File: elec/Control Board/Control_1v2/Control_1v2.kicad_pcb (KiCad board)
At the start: 2 copper layers, 205 x 190 mm, 348 parts, among them J1 DB9_Female_MountingHoles, J10 Conn_02x12_Odd_Even, J11 Con_01x02_2.5mm, J12 Con_01x02_2.5mm, J13 Con_01x02_2.5mm, J14 Conn_01x10, J15 DB25_Female_MountingHoles, J16 Conn_01x04, J17 Conn_01x05, J18 Conn_01x04, J19 Conn_01x07, J2 Conn_01x08, J20 Conn_01x04_KK-254_0470531000, J201 Con_01x02_2.5mm, J23 0.100_2Pin, J24 Conn_01x04, J25 Con_01x02_2.5mm, J26 Conn_01x10, J27 Conn_02x12_Odd_Even, J28 Con_01x02_2.5mm, J29 Conn_01x10, J3 Conn_01x08, J30 Con_01x02_2.5mm, J31 Con_01x02_2.5mm, J32 Con_01x02_2.5mm, J33 Con_01x02_2.5mm, J34 Con_01x02_2.5mm, J35 Conn_02x05_Odd_Even, J36 Conn_02x05_Odd_Even, J37 Conn_01x04, J38 Conn_02x06_Odd_Even, J39 Conn_02x06_Odd_Even, J4 Conn_01x08, J40 Conn_02x06_Odd_Even, J41 Conn_02x06_Odd_Even, J42 Conn_02x06_Odd_Even, J43 Conn_01x30, J44 Conn_01x30, J45 Conn_01x30, J46 Conn_01x30, J47 Conn_01x30, J48 Conn_01x30, J49 Conn_01x30, J5 Conn_01x08, J50 Conn_01x30, J51 Conn_01x30, J52 Conn_01x30, J53 Conn_01x30, J54 Conn_01x30, J55 Conn_02x06_Odd_Even, J56 Conn_02x06_Odd_Even, J57 Conn_02x06_Odd_Even, J58 Conn_02x06_Odd_Even, J59 Conn_02x06_Odd_Even, J6 Conn_01x08, J7 Conn_01x10, J8 Conn_02x18_Odd_Even, J801 Conn_01x03_0.1", J802 Con_01x02_0.1", J803 Screw_Terminal_01x04_5.08mm, J804 Screw_Terminal_01x02_5.08mm, J805 Con_01x02_0.1", J9 Conn_01x10, K801 Relay SRU-12VDC, Q1 BSS138, Q10 BSS138, Q11 BSS138, Q12 BSS138, Q13 BSS138, Q14 BSS138, Q2 NCE01P30K, Q3 BSS138, Q4 BSS138, Q801 BSS138, Q9 BSS138

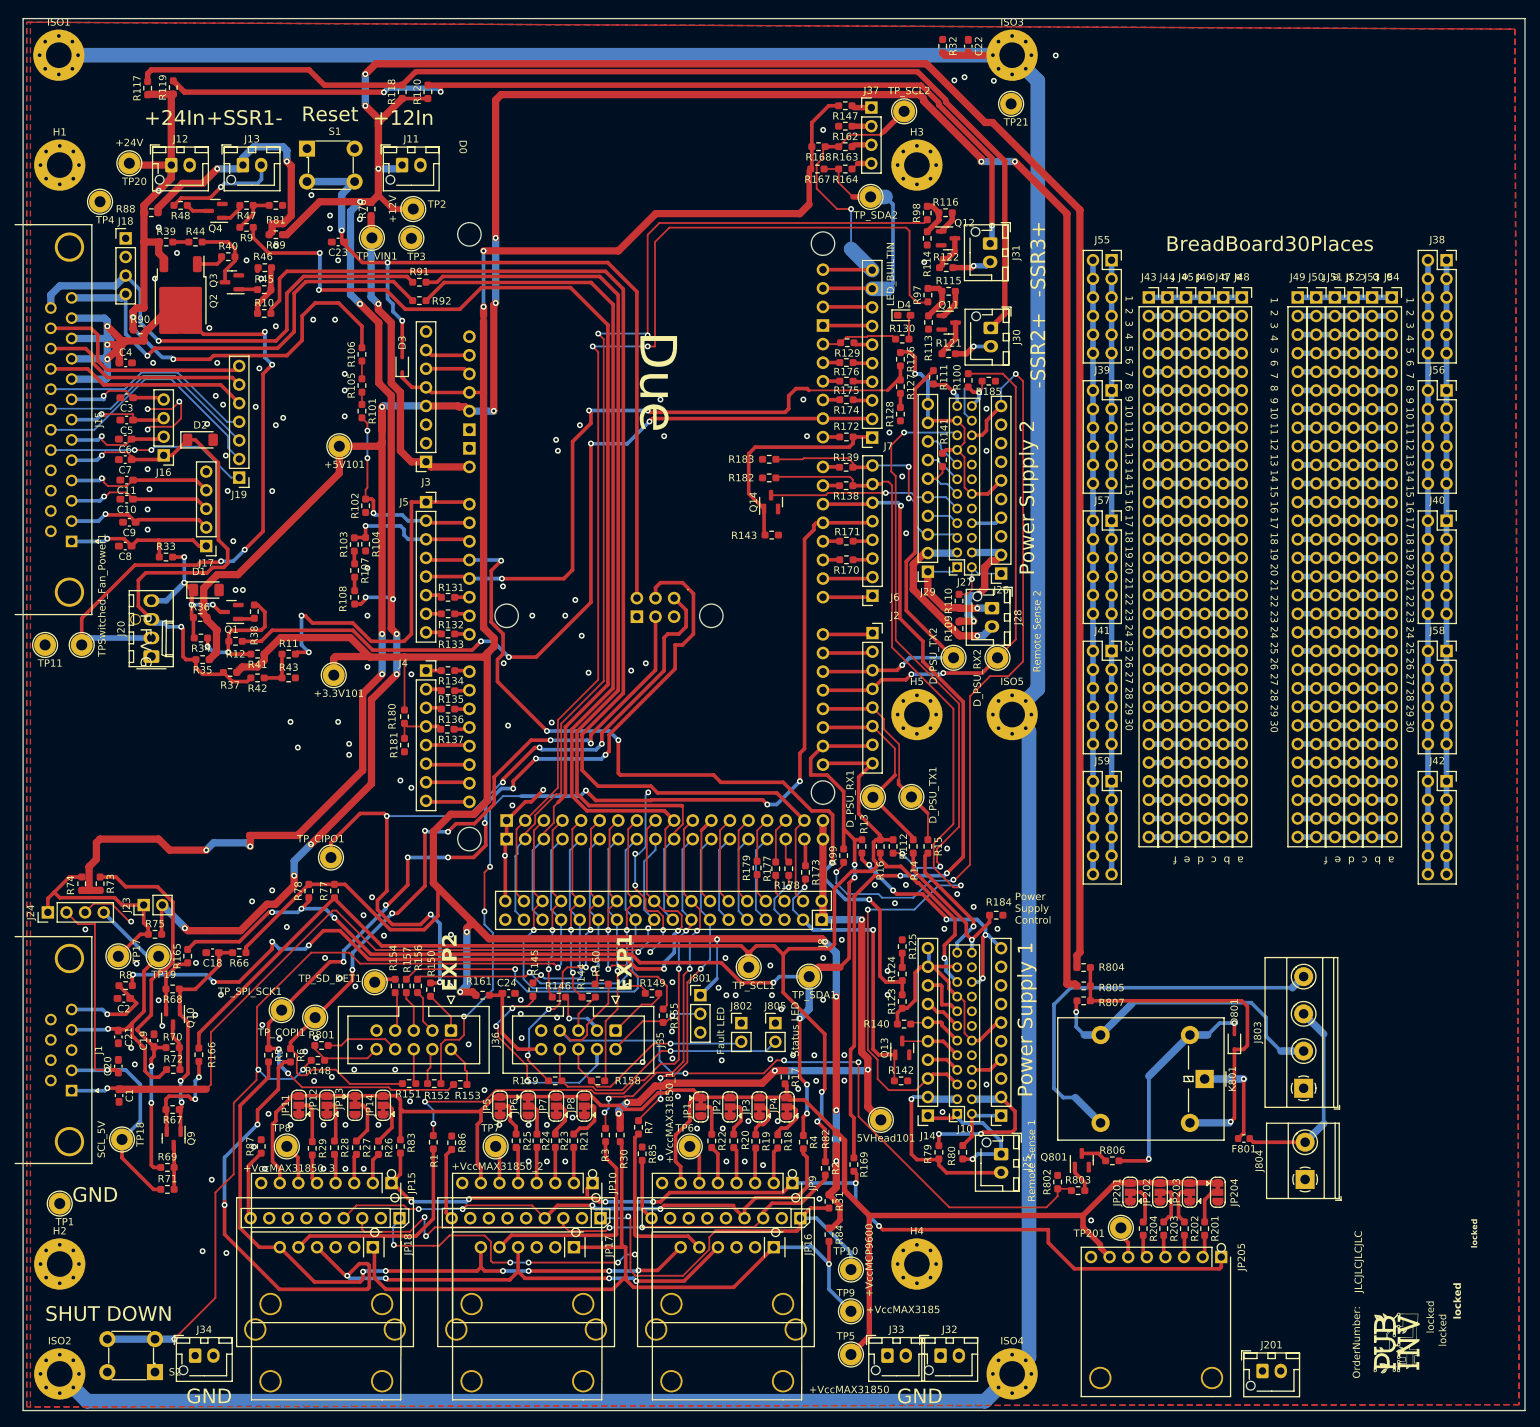
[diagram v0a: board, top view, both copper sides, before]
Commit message: PCB V1.2. Clear PCB errors. Plenty of warnings still.
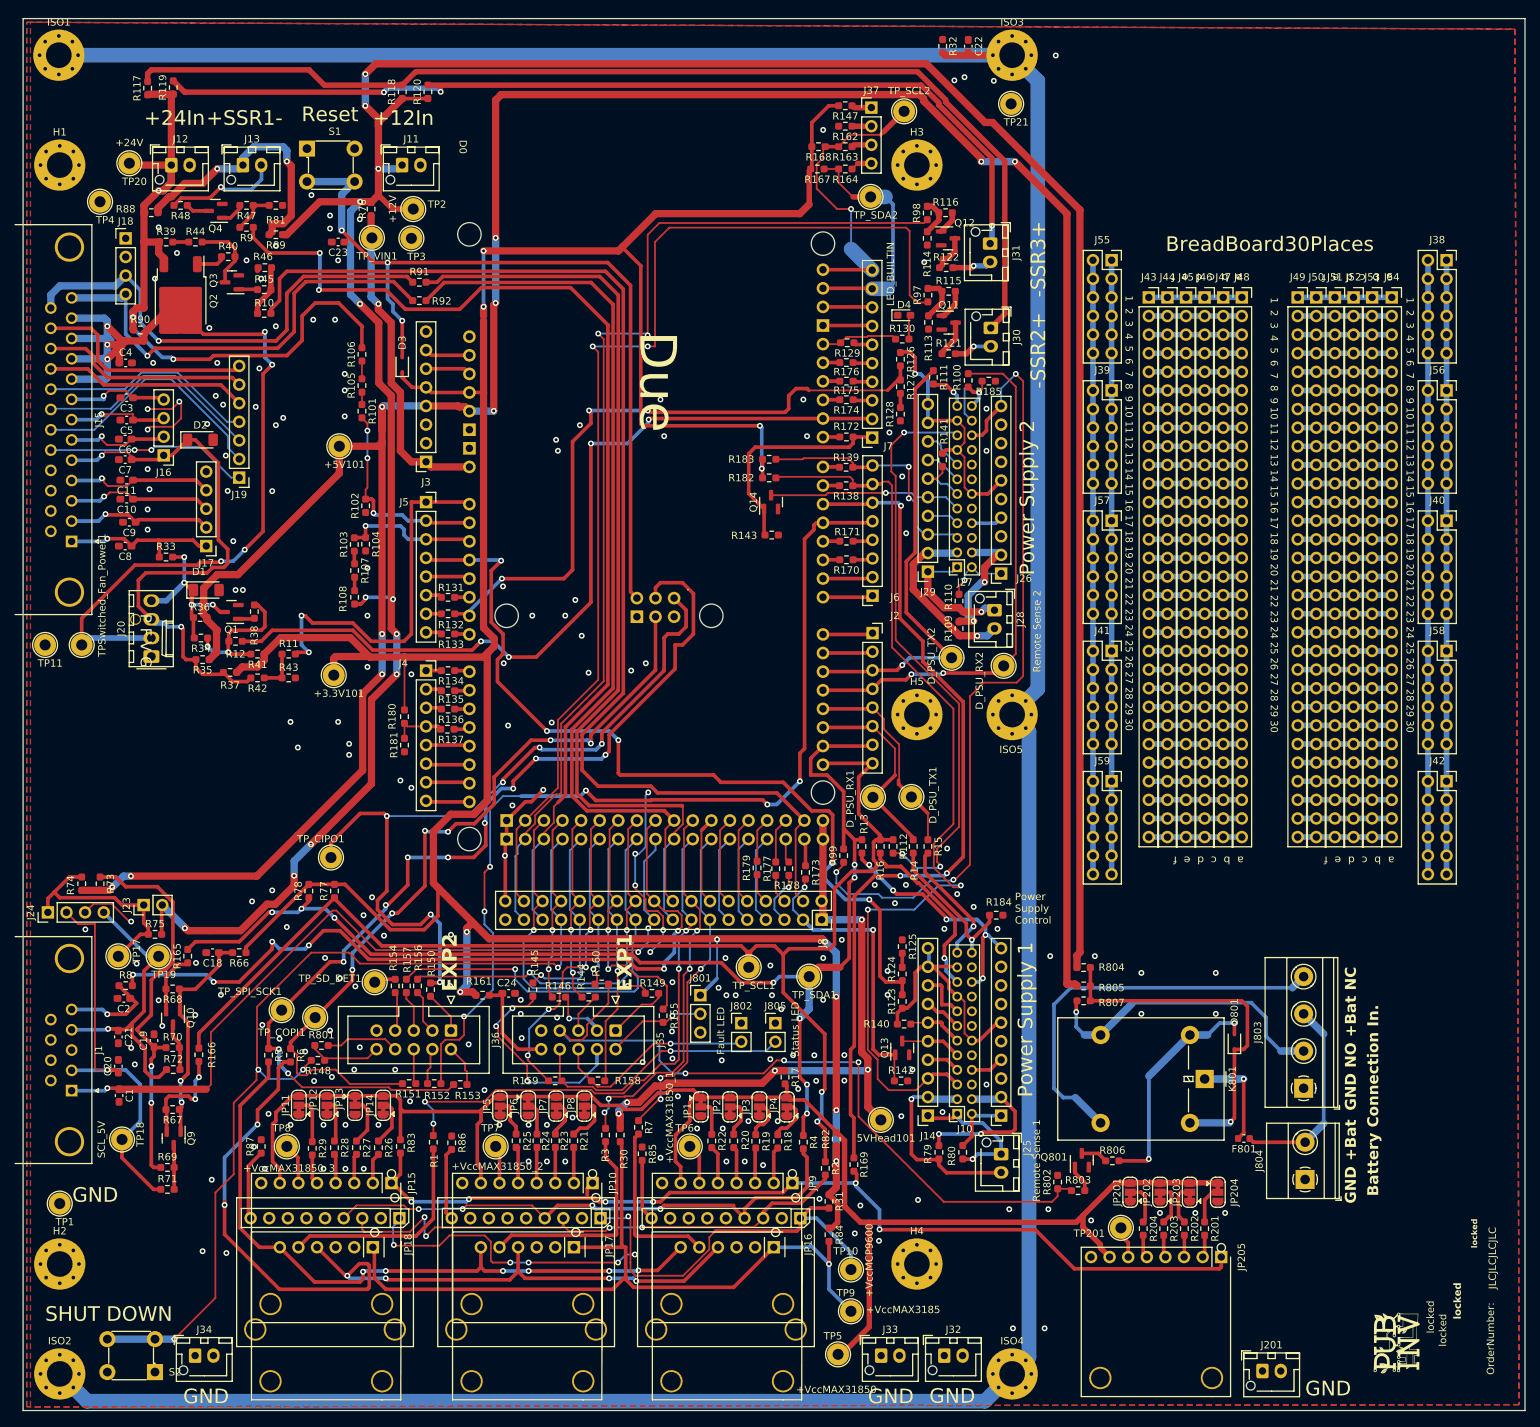
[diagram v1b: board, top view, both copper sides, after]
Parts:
- moved TP5 1.76 mm to (161.2, 217.3)
- moved D_PSU_RX2 1.39 mm to (183.8, 123.4)
- moved J33 0.86 mm to (167.1, 217.5)
- moved J32 0.51 mm to (175.7, 217.5)
- moved J28 0.44 mm to (182.6, 115.8)
- moved D_PSU_TX2 0.27 mm to (176.7, 122.2)
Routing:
- net +3.3V: track 379.8 -> 429.7 mm, vias 9 -> 11
- net +5V: track 402.4 -> 395.0 mm
- net Net-(J5-Pin_5): track 0.00 -> 6.04 mm
- net SENSE_AUX2: track 93.6 -> 90.1 mm
- net /Thermocouple Amplifier with 1-Wire Breakout Board - MAX31850K/+VccMAX31850: track 214.6 -> 216.7 mm
- net /PS2_SDA: track 107.7 -> 108.9 mm
- net /D_PSU_RX2: track 70.9 -> 72.1 mm
- net SPI_nRST: track 114.1 -> 113.2 mm
- net /Thermocouple Amplifier with 1-Wire Breakout Board - MAX31850K/DATA: track 133.5 -> 132.7 mm
- net +24V: track 98.1 -> 98.8 mm
- net /VO2+: track 9.47 -> 8.79 mm
- net /Display Interface/LED_Green: track 102.1 -> 101.5 mm
- net GND: vias 190 -> 209
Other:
- board text added: "Battery Connection In."
- board text added: "GND +Bat"
- board text added: "GND NO +Bat NC"
